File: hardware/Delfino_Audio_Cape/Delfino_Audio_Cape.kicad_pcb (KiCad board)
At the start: 2 copper layers, 143.8 x 162.6 mm, 141 parts, among them J1 JACK_PJ324, J1-J1 Conn_02x10_Odd_Even, J1-J2 Conn_02x10_Odd_Even, J1-J3 Conn_02x10_Odd_Even, J1-J4 Conn_02x10_Odd_Even, J2 JACK_PJ324, J3 JACK_PJ324, J4 PWR, J5 JACK_PJ324, J8 JACK_PJ324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

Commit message: Cambios en el PCB
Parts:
- added REF**: VIA-0.6mm, mi_via:VIA-0.6mm, F.Cu at (118.2, 213.2)
- added REF**: VIA-0.6mm, mi_via:VIA-0.6mm, F.Cu at (128.0, 213.0)
- added REF**: VIA-0.6mm, mi_via:VIA-0.6mm, F.Cu at (118.2, 158.6)
- added REF**: VIA-0.6mm, mi_via:VIA-0.6mm, F.Cu at (127.4, 158.2)
- moved R30 25.1 mm to (131.4, 218.8), turned to 90 degrees
- moved R31 24.8 mm to (135.0, 218.8), turned to 90 degrees
- moved R20 23.6 mm to (130.9, 161.5), turned to 90 degrees
- moved R21 23.2 mm to (134.4, 161.5), turned to 90 degrees
- moved C11 8.22 mm to (125.3, 148.7), turned to 270 degrees
- moved C17 8.06 mm to (125.9, 205.6), turned to 270 degrees
- moved TP6 8.02 mm to (140.8, 217.3)
- moved TP5 6.71 mm to (141.2, 160.7)
- moved TP3 6.53 mm to (141.4, 154.4)
- moved R15 4.31 mm to (118.1, 131.4)
- moved R26 4.24 mm to (129.0, 191.5), turned to 270 degrees
- moved TP4 3.84 mm to (140.8, 210.7)
- moved R16 3.53 mm to (128.3, 134.6), turned to 270 degrees
- moved R25 2.62 mm to (118.9, 188.7)
- moved R22 1.58 mm to (118.9, 183.8)
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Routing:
- net /Mic_2: track 35.5 -> 0.00 mm
- net +12V: track 670.1 -> 694.5 mm
- net /ADC_A3: track 99.1 -> 79.6 mm
- net GND: track 114.1 -> 133.3 mm
- net /ADC_A2: track 82.4 -> 68.4 mm
- net Net-(C11-Pad1): track 21.5 -> 22.7 mm
- net /Mic_Amp2/Voff: track 22.1 -> 21.0 mm
- net Net-(C17-Pad1): track 21.8 -> 22.7 mm
- net /Mic_Amp1/Voff: track 22.2 -> 21.7 mm

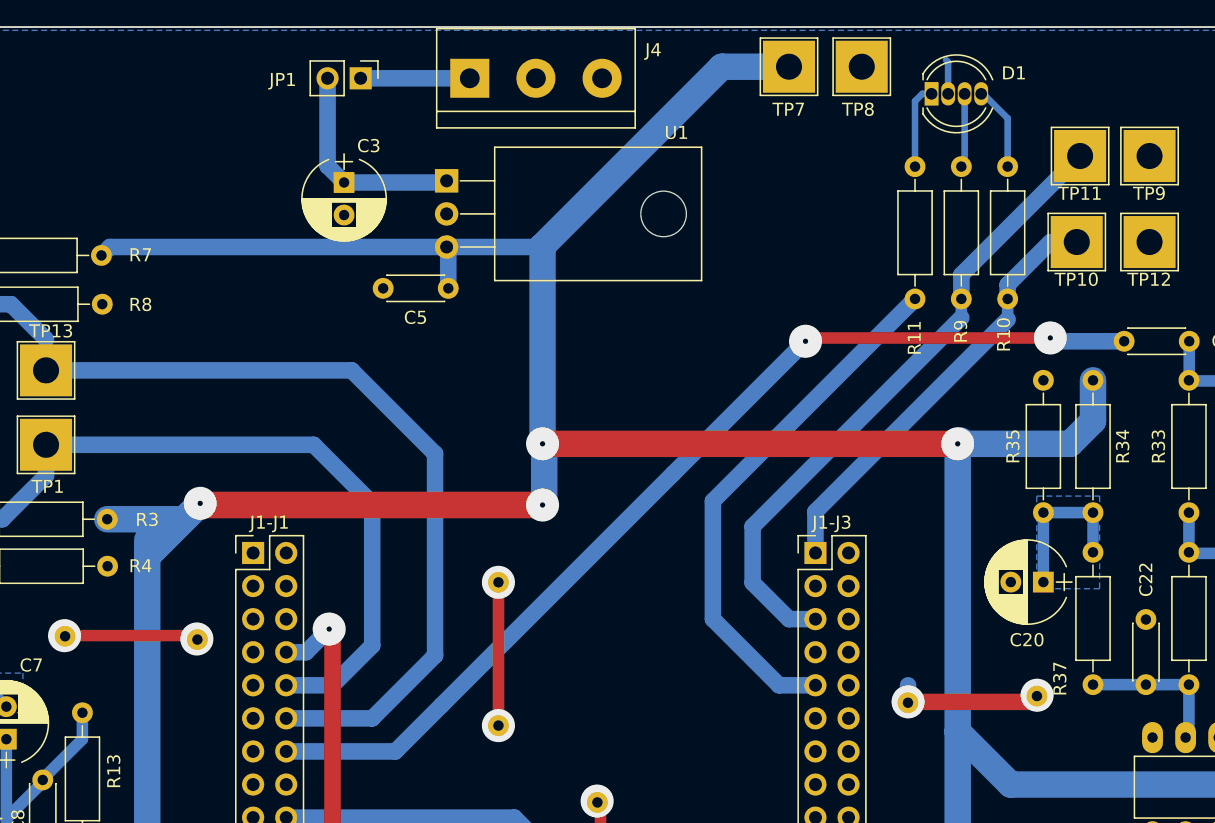
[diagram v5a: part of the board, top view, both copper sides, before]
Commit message: Cambios en el PCB de la tarjeta de expansión
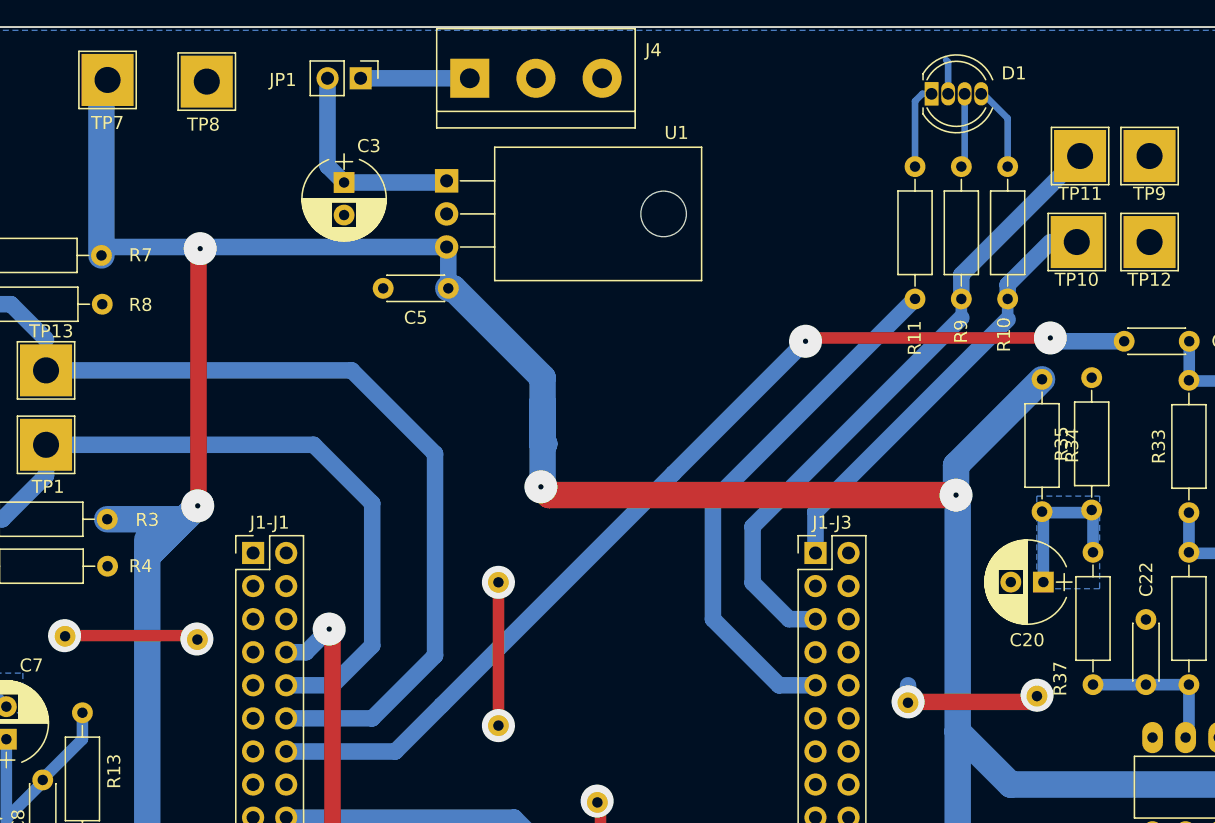
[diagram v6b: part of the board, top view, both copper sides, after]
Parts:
- moved TP7 52.3 mm to (145.3, 65.0)
- moved TP8 50.3 mm to (152.9, 65.2)
- moved R34 3.91 mm to (217.0, 88.0)
- moved R35 3.71 mm to (220.9, 98.0)
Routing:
- net +12V: track 694.5 -> 665.9 mm
